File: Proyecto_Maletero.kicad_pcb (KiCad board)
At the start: 2 copper layers, 65.2 x 59 mm, 49 parts, among them J1 DE9_Pins, J2 Conn_01x02, J3 Conn_01x02, J4 Conn_01x03, J5 Conn_01x02, J6 DE9_Pins, J7 Conn_01x04, J9 Conn_01x04, K1 FINDER-34.51, Q2 MMBT5550L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

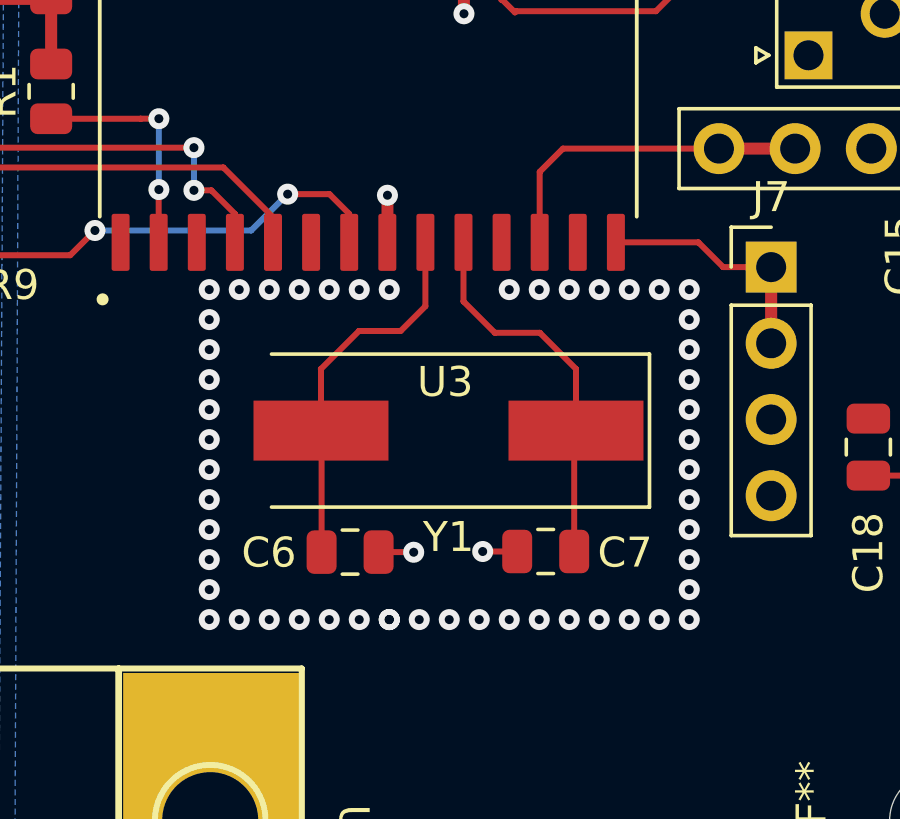
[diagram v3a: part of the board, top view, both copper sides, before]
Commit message: Ultimos ajustes de islas de gnd y huellas
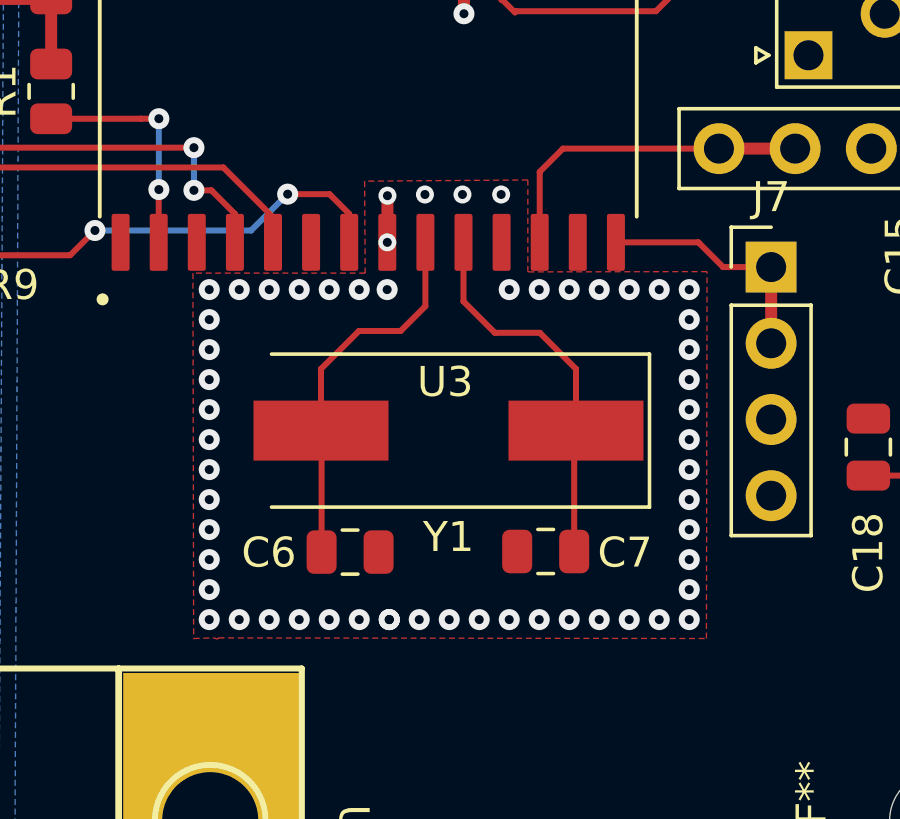
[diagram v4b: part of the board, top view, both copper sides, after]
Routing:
- net GND: track 16.1 -> 13.8 mm, vias 63 -> 65
- added copper zone on F.Cu, net GND
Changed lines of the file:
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@@
-	)
-	(segment
-		(start 149.51 127.07)
-		(end 149.515 127.075)
-		(width 0.2)
-		(layer "F.Cu")
-		(net 1)
 	)
 	(segment
@@
 	)
 	(segment
+		(start 148.64 116.74)
+		(end 148.635 116.745)
+		(width 0.4)
+		(layer "F.Cu")
+		(net 1)
+	)
+	(segment
 		(start 147.385 100.4458)
 		(end 147.385 100.7252)
@@
 	)
 	(segment
-		(start 148.64 116.74)
-		(end 148.635 116.745)
-		(width 0.4)
-		(layer "F.Cu")
-		(net 1)
-	)
-	(segment
 		(start 145.7198 101.3206)
 		(end 144.4346 101.3206)
@@
 	)
 	(segment
+		(start 148.64 115.19)
+		(end 148.64 116.74)
+		(width 0.4)
+		(layer "F.Cu")
+		(net 1)
+	)
+	(segment
 		(start 151.892 98.552)
 		(end 152.4 98.552)
@@
 	)
 	(segment
-		(start 151.815 127.05)
-		(end 152.965 127.05)
-		(width 0.2)
-		(layer "F.Cu")
-		(net 1)
-	)
-	(segment
 		(start 145.7198 100.2538)
 		(end 147.193 100.2538)
@@
 	)
 	(segment
-		(start 148.345 127.07)
-		(end 149.51 127.07)
-		(width 0.2)
-		(layer "F.Cu")
-		(net 1)
-	)
-	(segment
 		(start 168.93 118.11)
 		(end 167.45 118.11)
@@
 		(net 1)
 	)
-	(segment
-		(start 148.64 115.175)
-		(end 148.64 116.74)
-		(width 0.4)
-		(layer "F.Cu")
-		(net 1)
-	)
 	(via
 		(at 153.7 129.32)
@@
 	)
 	(via
-		(at 149.515 127.075)
-		(size 0.7)
-		(drill 0.3)
-		(layers "F.Cu" "B.Cu")
-		(free yes)
-		(net 1)
-	)
-	(via
 		(at 158.7 128.32)
 		(size 0.7)
@@
 	)
 	(via
+		(at 148.64 115.19)
+		(size 0.6)
+		(drill 0.3)
+		(layers "F.Cu" "B.Cu")
+		(free yes)
+		(net 1)
+	)
+	(via
 		(at 155.7 118.32)
 		(size 0.7)
@@
 	)
 	(via
-		(at 148.7 118.32)
+		(at 148.63 118.32)
 		(size 0.7)
 		(drill 0.3)
@@
 	)
 	(via
+		(at 149.89 115.15)
+		(size 0.6)
+		(drill 0.3)
+		(layers "F.Cu" "B.Cu")
+		(free yes)
+		(net 1)
+	)
+	(via
 		(at 142.7 128.32)
 		(size 0.7)
@@
 	)
 	(via
-		(at 148.64 115.175)
-		(size 0.7)
-		(drill 0.3)
-		(layers "F.Cu" "B.Cu")
-		(free yes)
-		(net 1)
-	)
-	(via
 		(at 146.7 129.32)
 		(size 0.7)
@@
 	)
 	(via
-		(at 151.815 127.05)
-		(size 0.7)
+		(at 152.43 115.15)
+		(size 0.6)
 		(drill 0.3)
 		(layers "F.Cu" "B.Cu")
@@
 	)
 	(via
+		(at 148.635 116.745)
+		(size 0.6)
+		(drill 0.3)
+		(layers "F.Cu" "B.Cu")
+		(net 1)
+	)
+	(via
 		(at 148.7 129.32)
 		(size 0.7)
@@
 		(at 166.26 124.52)
 		(size 0.7)
+		(drill 0.3)
+		(layers "F.Cu" "B.Cu")
+		(free yes)
+		(net 1)
+	)
+	(via
+		(at 151.14 115.15)
+		(size 0.6)
 		(drill 0.3)
 		(layers "F.Cu" "B.Cu")
@@
 	)
 	(zone
+		(net 1)
+		(net_name "GND")
+		(layer "F.Cu")
+		(hatch edge 0.5)
+		(priority 4)
+		(connect_pads
+			(clearance 0.5)
+		)
+		(min_thickness 0.25)
+		(filled_areas_thickness no)
+		(fill yes
+			(thermal_gap 0.5)
+			(thermal_bridge_width 0.5)
+		)
+		(polygon
+			(pts
+				(xy 143.01 129.93) (xy 159.27304 129.950744) (xy 159.294055 117.719983) (xy 153.32 117.729891) (xy 153.32 114.666615)
+				(xy 147.878384 114.704938) (xy 147.897783 117.77) (xy 142.156085 117.77) (xy 142.18 129.95) (xy 142.85 129.93)
+				(xy 142.97 129.97)
+			)
+		)
+	)
+	(zone

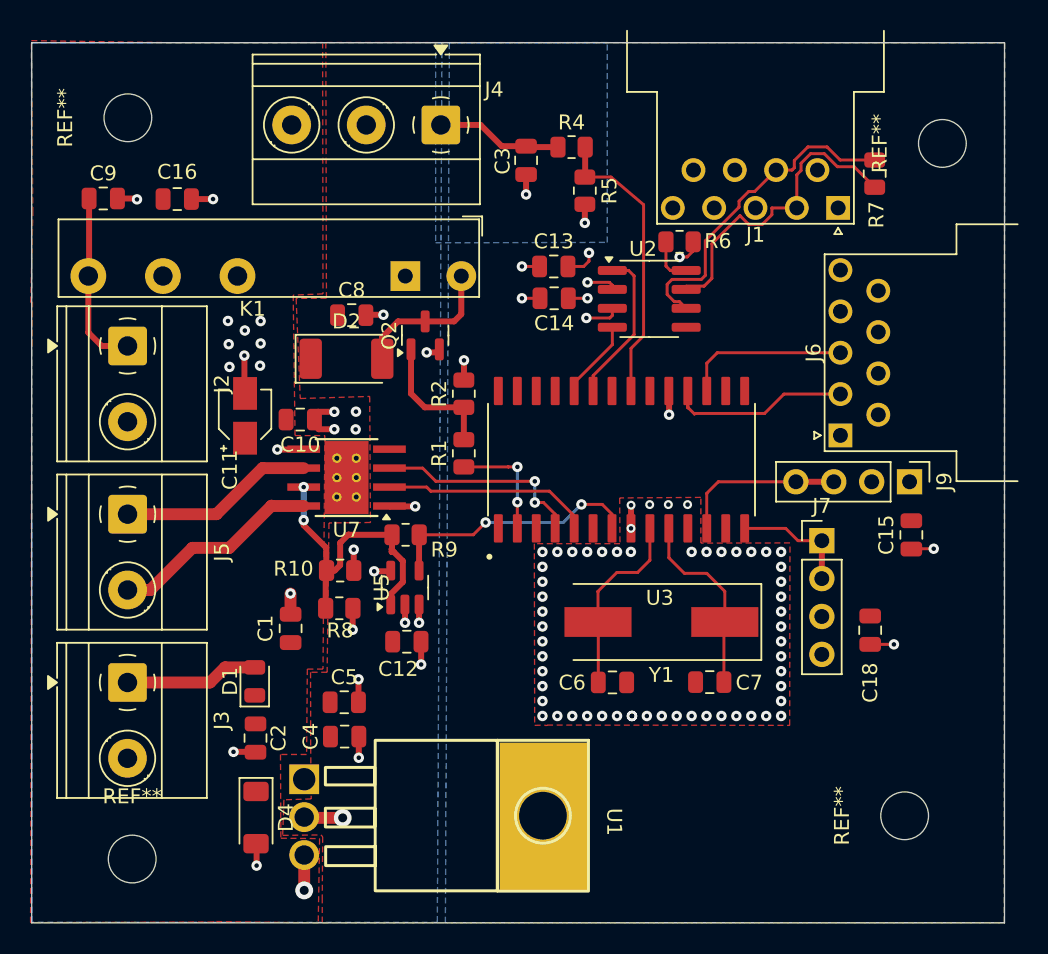
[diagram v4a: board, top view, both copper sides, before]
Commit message: DRC errores 0 warnings 25
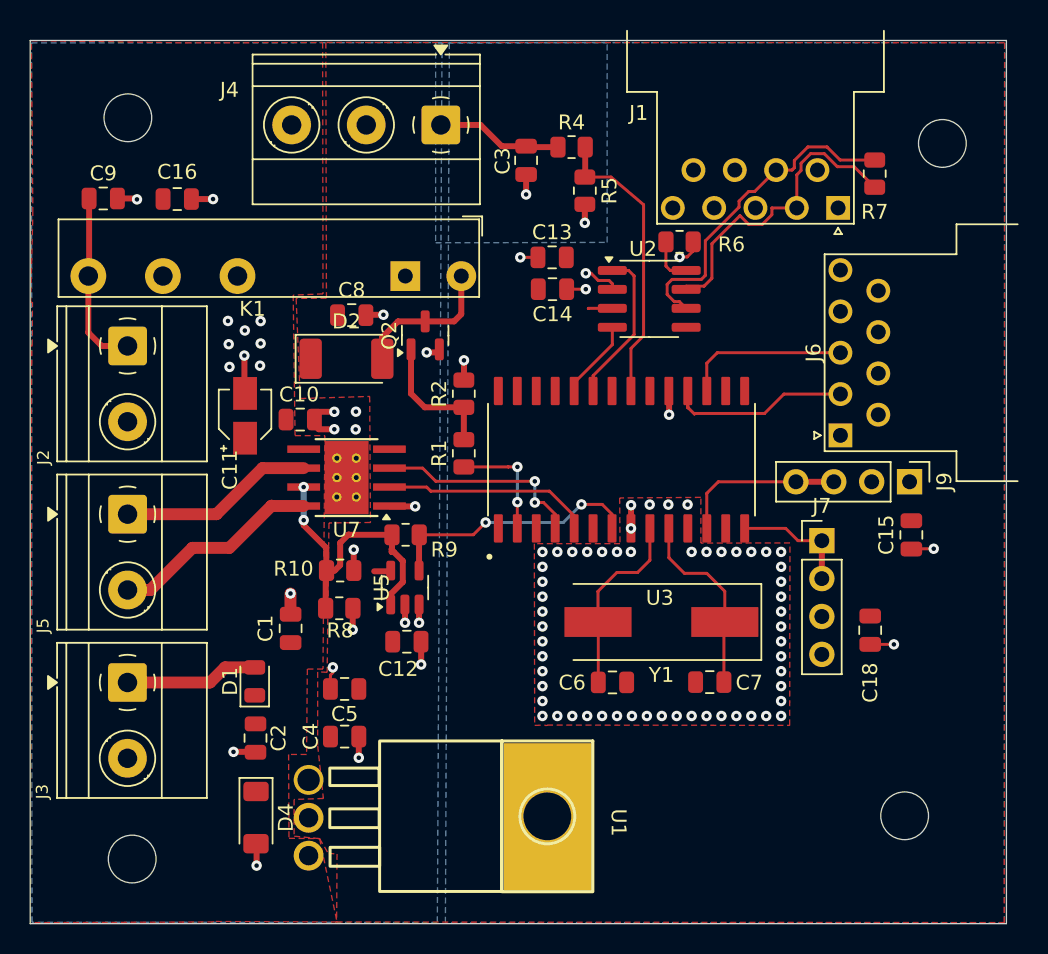
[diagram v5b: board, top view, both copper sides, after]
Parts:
- moved C5 0.89 mm to (129.4, 127.5), turned to 180 degrees
- moved C13 0.62 mm to (143.3, 98.6)
- moved C14 0.62 mm to (143.4, 100.7)
- moved U1 0.30 mm to (151.6, 136.1)
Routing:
- net VCC: track 9.52 -> 2.92 mm, vias 5 -> 0
- net VBAT: track 4.42 -> 0.31 mm, vias 2 -> 0
- net GND: track 13.8 -> 14.2 mm, vias 65 -> 64
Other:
- board size 65.2 x 59 mm -> 65.4 x 59.2 mm

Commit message: actu
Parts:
- moved C5 0.30 mm to (129.5, 127.8), turned to 0 degrees
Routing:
- net VCC: track 2.92 -> 1.86 mm
- net GNDPWR: track 29.4 -> 29.3 mm, vias 29 -> 31
- added copper zone on F.Cu, net GNDPWR
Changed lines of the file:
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@@
 		(at 151.6254 136.144 -90)
 		(property "Reference" "U1"
-			(at 0.32 3.82 270)
+			(at -0.074 3.6754 270)
 			(unlocked yes)
 			(layer "F.SilkS")
@@
 		(tags "capacitor")
 		(property "Reference" "C8"
-			(at 0 -1.68 0)
+			(at -2.745 0.01 0)
 			(layer "F.SilkS")
 			(effects
@@
 		(tags "Diode MELF ")
 		(property "Reference" "D2"
-			(at 0 -2.5 0)
+			(at 0.305 2.375 0)
 			(layer "F.SilkS")
 			(effects
@@
 		(tags "SOT TO_SOT_SMD")
 		(property "Reference" "U5"
-			(at 0 -1.56 90)
+			(at -0.4 2.48 90)
 			(layer "F.SilkS")
 			(effects
@@
 		(tags "Through hole pin header THT 1x04 2.54mm single row")
 		(property "Reference" "J7"
-			(at 0 -2.33 0)
+			(at 2.75 1.81 0)
 			(layer "F.SilkS")
 			(effects
@@
 	(footprint "Capacitor_SMD:C_0805_2012Metric"
 		(layer "F.Cu")
-		(at 129.4384 127.508 180)
+		(at 129.54 127.79)
 		(descr "Capacitor SMD 0805 (2012 Metric), square (rectangular) end terminal, IPC_7351 nominal, (Body size source: IPC-SM-782 page 76, https://www.pcb-3d.com/wordpress/wp-content/uploads/ipc-sm-782a_amendment_1_and_2.pdf, https://docs.google.com/spreadsheets/d/1BsfQQcO9C6DZCsRaXUlFlo91Tg2WpOkGARC1WS5S8t0/edit?usp=sharing), generated with kicad-footprint-generator")
 		(tags "capacitor")
@@
 		)
 		(property "Datasheet" ""
-			(at 0 0 180)
+			(at 0 0 0)
 			(unlocked yes)
 			(layer "F.Fab")
@@
 		)
 		(property "Description" "Polarized capacitor, US symbol"
-			(at 0 0 180)
+			(at 0 0 0)
 			(unlocked yes)
 			(layer "F.Fab")
@@
 		(attr smd)
 		(fp_line
-			(start -0.261252 0.735)
-			(end 0.261252 0.735)
+			(start -0.261252 -0.735)
+			(end 0.261252 -0.735)
 			(stroke
 				(width 0.12)
@@
 		)
 		(fp_line
-			(start -0.261252 -0.735)
-			(end 0.261252 -0.735)
+			(start -0.261252 0.735)
+			(end 0.261252 0.735)
 			(stroke
 				(width 0.12)
@@
 		)
 		(fp_line
-			(start 1.7 0.98)
-			(end -1.7 0.98)
+			(start -1.7 -0.98)
+			(end 1.7 -0.98)
 			(stroke
 				(width 0.05)
@@
 		)
 		(fp_line
-			(start 1.7 -0.98)
-			(end 1.7 0.98)
+			(start -1.7 0.98)
+			(end -1.7 -0.98)
 			(stroke
 				(width 0.05)
@@
 		)
 		(fp_line
-			(start -1.7 0.98)
-			(end -1.7 -0.98)
+			(start 1.7 -0.98)
+			(end 1.7 0.98)
 			(stroke
 				(width 0.05)
@@
 		)
 		(fp_line
-			(start -1.7 -0.98)
-			(end 1.7 -0.98)
+			(start 1.7 0.98)
+			(end -1.7 0.98)
 			(stroke
 				(width 0.05)
@@
 		)
 		(fp_line
-			(start 1 0.625)
-			(end -1 0.625)
+			(start -1 -0.625)
+			(end 1 -0.625)
 			(stroke
 				(width 0.1)
@@
 		)
 		(fp_line
-			(start 1 -0.625)
-			(end 1 0.625)
+			(start -1 0.625)
+			(end -1 -0.625)
 			(stroke
 				(width 0.1)
@@
 		)
 		(fp_line
-			(start -1 0.625)
-			(end -1 -0.625)
+			(start 1 -0.625)
+			(end 1 0.625)
 			(stroke
 				(width 0.1)
@@
 		)
 		(fp_line
-			(start -1 -0.625)
-			(end 1 -0.625)
+			(start 1 0.625)
+			(end -1 0.625)
 			(stroke
 				(width 0.1)
@@
 		)
 		(pad "1" smd roundrect
-			(at -0.95 0 180)
+			(at -0.95 0)
 			(size 1 1.45)
 			(layers "F.Cu" "F.Mask" "F.Paste")
@@
 		)
 		(pad "2" smd roundrect
-			(at 0.95 0 180)
+			(at 0.95 0)
 			(size 1 1.45)
 			(layers "F.Cu" "F.Mask" "F.Paste")
@@
 		(tags "Capacitor Electrolytic")
 		(property "Reference" "C11"
-			(at -3.62 -1.015 90)
+			(at 3.65 2.455 90)
 			(layer "F.SilkS")
 			(effects
@@
 		(tags "SOT TO_SOT_SMD")
 		(property "Reference" "Q2"
-			(at 0 -2.4 90)
+			(at -0.0225 3 90)
 			(layer "F.SilkS")
 			(effects
@@
 		(tags "Through hole pin header THT 1x04 2.54mm single row")
 		(property "Reference" "J9"
-			(at 0 -2.33 90)
+			(at -2.53 7.71 180)
 			(layer "F.SilkS")
 			(effects
@@
 	)
 	(segment
-		(start 128.651 126.0602)
-		(end 128.651 126.4158)
-		(width 0.2)
-		(layer "F.Cu")
-		(net 43)
-	)
-	(segment
 		(start 127.415 109.45)
 		(end 127.415 109.8128)
@@
 	)
 	(segment
-		(start 128.651 126.4158)
-		(end 128.4884 126.5784)
-		(width 0.2)
-		(layer "F.Cu")
-		(net 43)
-	)
-	(segment
 		(start 122.72 107.655)
 		(end 122.765 107.7)
@@
 	)
 	(segment
-		(start 128.4884 126.5784)
-		(end 128.4884 127.508)
-		(width 0.2)
-		(layer "F.Cu")
-		(net 43)
-	)
-	(segment
 		(start 145.542 96.266)
 		(end 145.542 95.0195)
@@
 	)
 	(segment
+		(start 131.93 127.79)
+		(end 130.49 127.79)
+		(width 0.4)
+		(layer "F.Cu")
+		(net 43)
+	)
+	(segment
 		(start 129.98 123.54)
 		(end 129.98 122.115)
@@
 	)
 	(via
-		(at 128.651 126.0602)
+		(at 131.93 127.79)
 		(size 0.7)
 		(drill 0.3)
@@
 	)
 	(via
+		(at 131.4 118.15)
+		(size 0.6)
+		(drill 0.3)
+		(layers "F.Cu" "B.Cu")
+		(free yes)
+		(net 43)
+	)
+	(via
 		(at 121.99 131.725)
 		(size 0.7)
@@
 		(net 43)
 	)
+	(via
+		(at 130.75 118.15)
+		(size 0.6)
+		(drill 0.3)
+		(layers "F.Cu" "B.Cu")
+		(free yes)
+		(net 43)
+	)
 	(segment
 		(start 147.385 101.9952)
@@
 	)
 	(segment
-		(start 132.4825 119.62)
-		(end 132.53 119.5725)
+		(start 128.49 127.5096)
+		(end 128.4884 127.508)
 		(width 0.4)
 		(layer "F.Cu")
@@
 	)
 	(segment
-		(start 131.42 119.62)
-		(end 132.4825 119.62)
+		(start 132.4825 119.62)
+		(end 132.53 119.5725)
 		(width 0.4)
 		(layer "F.Cu")
@@
 	)
 	(zone
+		(net 43)
+		(net_name "GNDPWR")
+		(layer "F.Cu")
+		(hatch edge 0.5)
+		(priority 5)
+		(connect_pads
+			(clearance 0.5)
+		)
+		(min_thickness 0.25)
+		(filled_areas_thickness no)
+		(fill yes
+			(thermal_gap 0.5)
+			(thermal_bridge_width 0.5)
+		)
+		(polygon
+			(pts
+				(xy 121.19 102.36) (xy 124.16 102.38) (xy 124.21 106.32) (xy 121.2 106.32)
+			)
+		)
+	)
+	(zone
 		(net 1)
 		(net_name "GND")
@@
 	)
 	(zone
+		(net 43)
+		(net_name "GNDPWR")
+		(layer "F.Cu")
+		(hatch edge 0.5)
+		(priority 6)
+		(connect_pads
+			(clearance 0.5)
+		)
+		(min_thickness 0.25)
+		(filled_areas_thickness no)
+		(fill yes
+			(thermal_gap 0.5)
+			(thermal_bridge_width 0.5)
+		)
+		(polygon
+			(pts
+				(xy 128.53 108.45) (xy 130.54 108.45) (xy 130.52 110.48) (xy 128.54 110.47)
+			)
+		)
+	)
+	(zone
 		(net 44)
 		(net_name "VCC")
@@
 			)
 		)
+	)
+	(zone
+		(net 43)
+		(net_name "GNDPWR")
+		(layer "F.Cu")
+		(hatch edge 0.5)
+		(priority 7)
+		(connect_pads
+			(clearance 0.5)
+		)
+		(min_thickness 0.25)
+		(filled_areas_thickness no)
+		(fill yes
+			(thermal_gap 0.5)
+			(thermal_bridge_width 0.5)
+		)
+		(polygon
+			(pts
+				(xy 129.675 117.65) (xy 131.725 117.65) (xy 131.774965 118.57619) (xy 129.625 118.525) (xy 129.625 118)
+			)
+		)

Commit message: Correccion de errores en clase
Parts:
- moved C13 10.1 mm to (151.0, 105.2), turned to 180 degrees
- moved R7 8.12 mm to (158.9, 98.3), turned to 180 degrees
- moved C12 3.99 mm to (132.6, 120.5), turned to -90 degrees
- moved C5 3.50 mm to (132.9, 128.6)
- moved R9 2.50 mm to (136.0, 116.8)
- moved U5 2.45 mm to (135.9, 120.6)
- moved C14 1.62 mm to (144.3, 102.0), turned to 0 degrees
- moved C1 1.12 mm to (124.8, 122.9)
- moved D4 0.55 mm to (123.0, 136.0)
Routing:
- net CAN+: track 21.3 -> 16.0 mm
- net CAN-: track 22.3 -> 17.4 mm
- net GNDPWR: track 29.3 -> 33.8 mm, vias 31 -> 39
- net SENSE: track 20.5 -> 23.8 mm
- net VCC: track 1.86 -> 4.77 mm
- net Vopam: track 17.4 -> 15.1 mm
- net GND: track 14.2 -> 12.8 mm

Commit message: Modificaciones de Clase
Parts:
- moved J9 11.6 mm to (165.4, 125.1), turned to 180 degrees
- moved C15 8.18 mm to (169.2, 125.2), turned to 180 degrees
- moved C18 6.36 mm to (161.5, 129.1)
- moved R8 3.94 mm to (129.1, 118.2), turned to -90 degrees
- moved R10 2.80 mm to (126.7, 118.2), turned to 90 degrees
- moved J6 2.30 mm to (160.8, 111.8)
- moved C1 1.43 mm to (123.4, 123.0)
- moved REF** 0.99 mm to (168.5, 90.8)
- moved C12 0.28 mm to (132.9, 120.5)
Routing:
- net SENAL_RELE: track 11.2 -> 17.2 mm
- net SENSE: track 23.8 -> 18.0 mm
- net GNDPWR: track 33.8 -> 30.5 mm, vias 39 -> 44
- net TX_USART: track 11.1 -> 8.37 mm
- net RX_USART: track 12.1 -> 9.59 mm
- net GND: track 12.8 -> 14.4 mm
